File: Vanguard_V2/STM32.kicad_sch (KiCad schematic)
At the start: 11 parts, among them U1 STM32H743VITx, Y1 LFXTAL078719Cutt

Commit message: V2 Board Ready
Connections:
- net SERVO_5_PWM: now reaches U1.2 (PE3)
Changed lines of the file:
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@@
+	(wire
+		(pts
+			(xy 52.07 81.28) (xy 54.61 81.28)
+		)
+		(stroke
+			(width 0)
+			(type default)
+		)
+	)
 	(wire
 		(pts
@@
 				(hide yes)
 			)
+		)
+	)
+	(global_label "SERVO_5_PWM"
+		(shape input)
+		(at 52.07 81.28 180)
+		(fields_autoplaced yes)
+		(effects
+			(font
+				(size 1.27 1.27)
+			)
+			(justify right)
+		)
+		(property "Intersheetrefs" "${INTERSHEET_REFS}"
+			(at 35.7197 81.28 0)
+			(effects
+				(font
+					(size 1.27 1.27)
+				)
+				(justify right)
+				(hide yes)
+			)

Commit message: started layout for V2.1
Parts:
- removed C5, C6: 20pF, Capacitor_SMD:C_0402_1005Metric, symbol Device:C
- removed Y1: LFXTAL078719Cutt, VanguardLib:LFXTAL078719Cutt, symbol VanguardLib:LFXTAL078719Cutt
- added X1: ECS-2520MV-xxx-xx, Oscillator:Oscillator_SMD_ECS_2520MV-xxx-xx-4Pin_2.5x2.0mm, symbol Oscillator:ECS-2520MV-xxx-xx
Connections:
- net +3.3V: now also X1.1 (Tri-State), X1.4 (VDD)
- net GND: now also X1.2 (GND)
- net OSC32_IN: no longer names the net of U1.8 (PC14)
- net OSC32_OUT: no longer names the net of U1.9 (PC15)
- net OSC_IN renamed HSE_BYPASS
- net HSE_BYPASS: now also X1.3 (OUT)
- net OSC_OUT: no longer names the net of U1.13 (PH1)

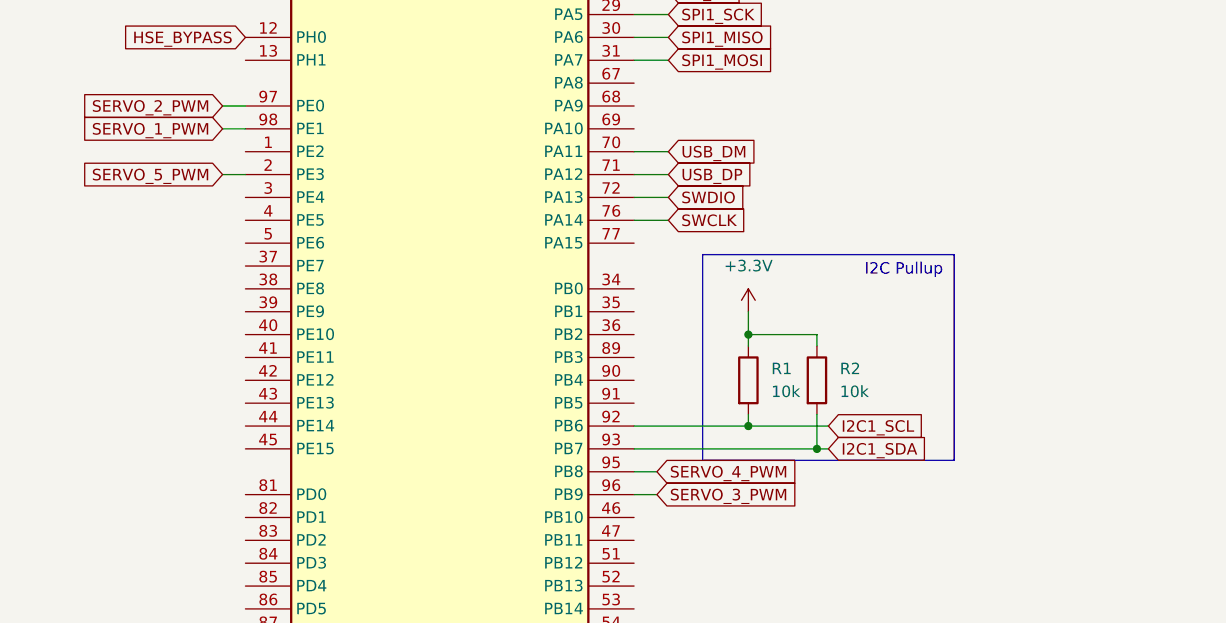
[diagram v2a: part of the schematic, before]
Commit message: Begun board routing
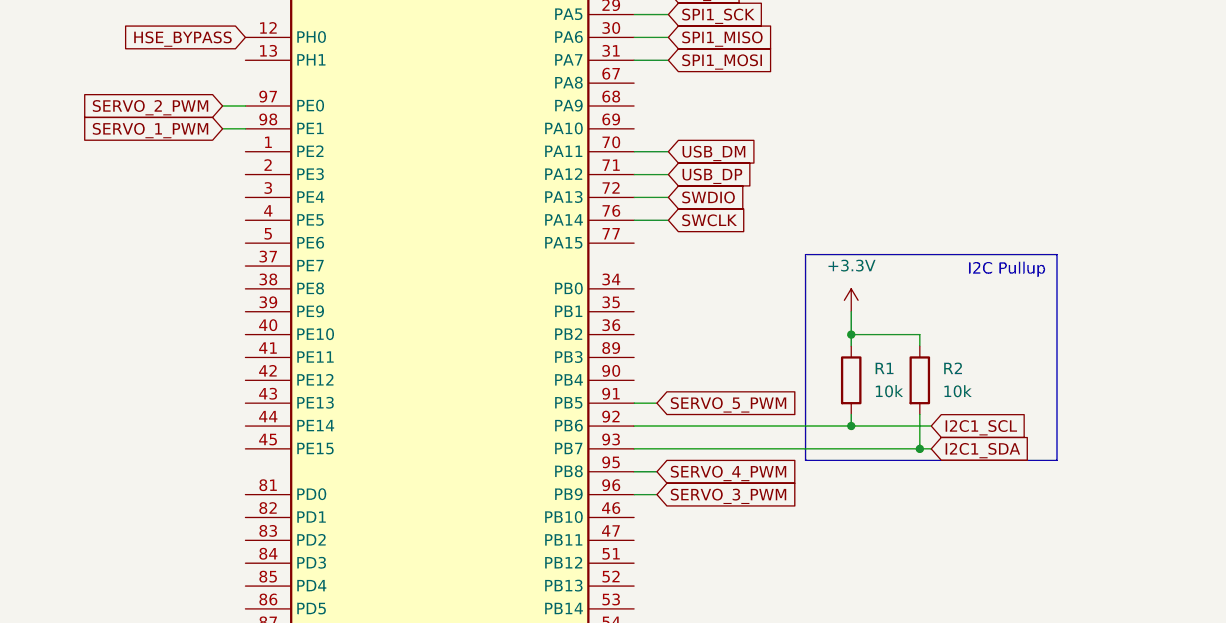
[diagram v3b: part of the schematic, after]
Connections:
- net SERVO_5_PWM: now also U1.91 (PB5); no longer U1.2 (PE3)
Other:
- moved on the sheet: R1, R2

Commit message: Everything is placed
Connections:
- net C2_GATE: now reaches U1.15 (PC0)
- net C1_GATE: now reaches U1.24 (PA2)
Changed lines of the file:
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@@
+	(wire
+		(pts
+			(xy 97.79 55.88) (xy 101.6 55.88)
+		)
+		(stroke
+			(width 0)
+			(type default)
+		)
+	)
 	(wire
 		(pts
@@
 		(pts
 			(xy 120.65 31.75) (xy 115.57 31.75)
+		)
+		(stroke
+			(width 0)
+			(type default)
+		)
+	)
+	(wire
+		(pts
+			(xy 97.79 137.16) (xy 100.33 137.16)
 		)
 		(stroke
@@
 		)
 	)
+	(global_label "C2_GATE"
+		(shape input)
+		(at 100.33 137.16 0)
+		(fields_autoplaced yes)
+		(effects
+			(font
+				(size 1.27 1.27)
+			)
+			(justify left)
+		)
+		(property "Intersheetrefs" "${INTERSHEET_REFS}"
+			(at 111.2375 137.16 0)
+			(effects
+				(font
+					(size 1.27 1.27)
+				)
+				(justify left)
+				(hide yes)
+			)
+		)
+	)
 	(global_label "SERVO_3_PWM"
 		(shape input)
@@
 			(effects
 				(font
+					(size 1.27 1.27)
+				)
+				(justify left)
+				(hide yes)
+			)
+		)
+	)
+	(global_label "C1_GATE"
+		(shape input)
+		(at 101.6 55.88 0)
+		(fields_autoplaced yes)
+		(effects
+			(font
+				(size 1.27 1.27)
+			)
+			(justify left)
+		)
+		(property "Intersheetrefs" "${INTERSHEET_REFS}"
+			(at 112.5075 55.88 0)
+			(effects
+				(font

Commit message: Added ejection charges
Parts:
- added TP1, TP2, TP3, TP4: TestPoint, Connector_Wire:SolderWirePad_1x01_SMD_1x2mm, symbol Connector:TestPoint
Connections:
- net at U1.56 (PD9): now also TP4.1
- net at U1.63 (PC6): now also TP3.1
- net at U1.64 (PC7): now also TP2.1
- net at U1.65 (PC8): now also TP1.1

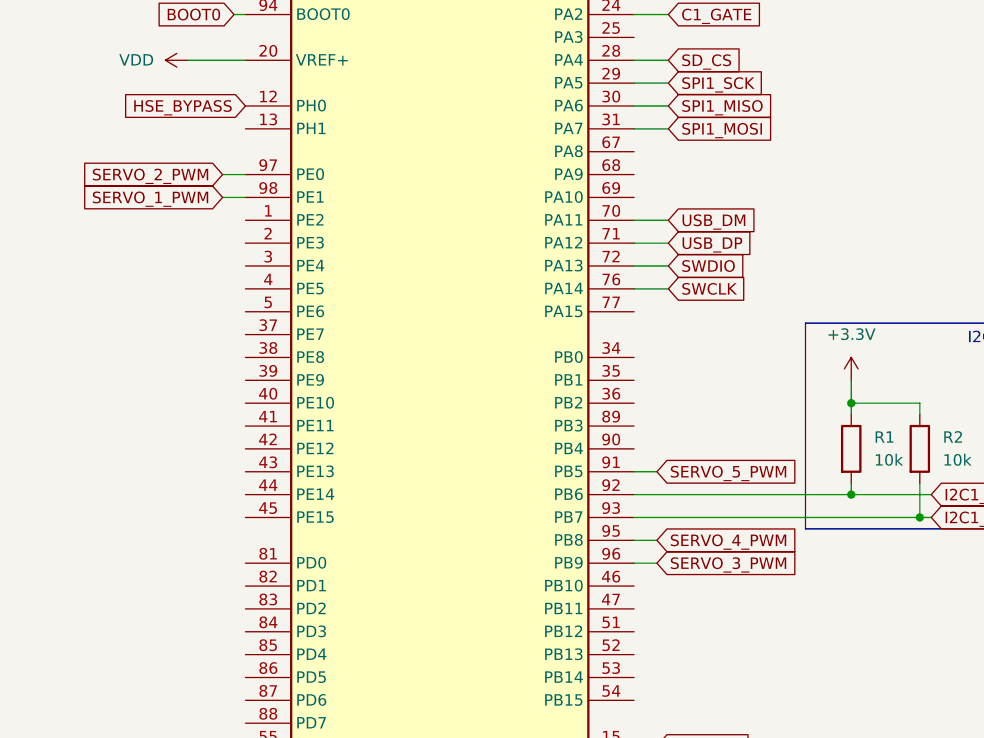
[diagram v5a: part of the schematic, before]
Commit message: Fixed sensors
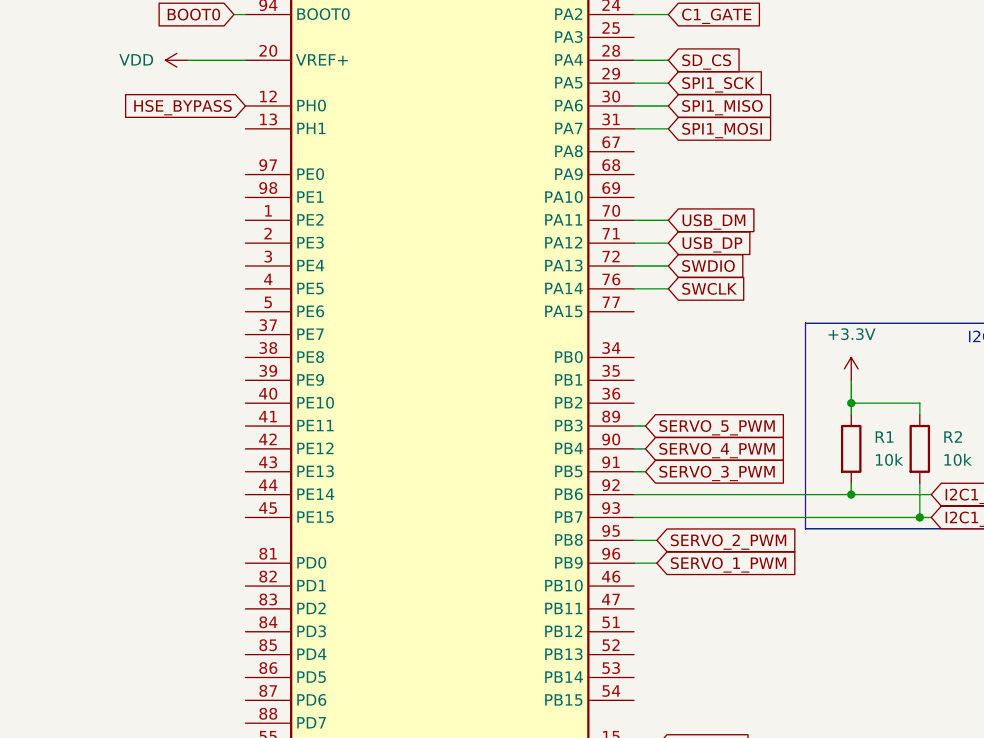
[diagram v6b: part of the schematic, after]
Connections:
- net SERVO_1_PWM: now also U1.96 (PB9); no longer U1.98 (PE1)
- net SERVO_2_PWM: now also U1.95 (PB8); no longer U1.97 (PE0)
- net SERVO_3_PWM: now also U1.91 (PB5); no longer U1.96 (PB9)
- net SERVO_4_PWM: now also U1.90 (PB4); no longer U1.95 (PB8)
- net SERVO_5_PWM: now also U1.89 (PB3); no longer U1.91 (PB5)
